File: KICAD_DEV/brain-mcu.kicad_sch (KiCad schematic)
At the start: 22 parts, among them SW1 SW_Push, SW2 SW_Push, U1 STM32H743VITx, Y1 8 MHz, Y2 32.768 KHz

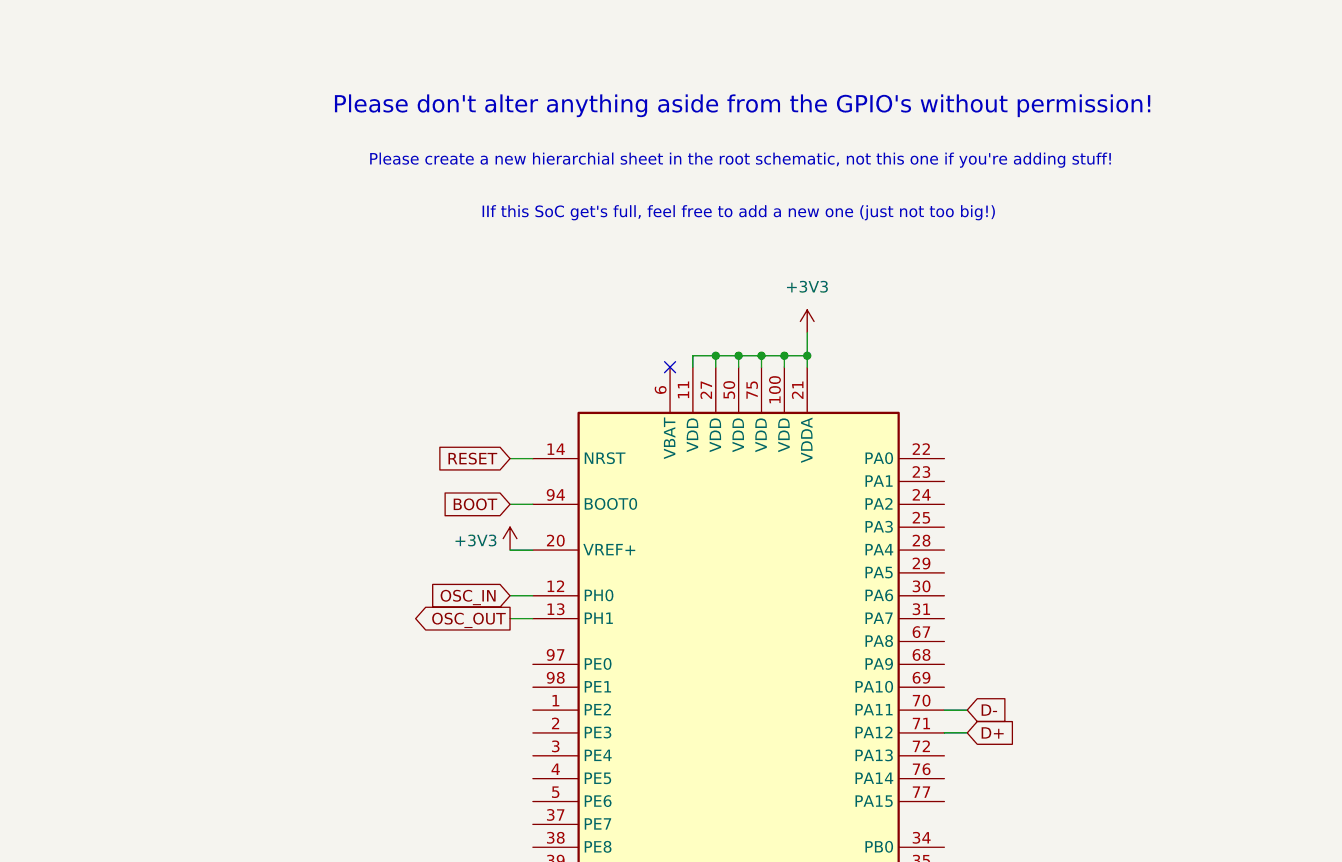
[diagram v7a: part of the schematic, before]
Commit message: wired the TMC2209 to my MCU, also more instructions on the schematic!
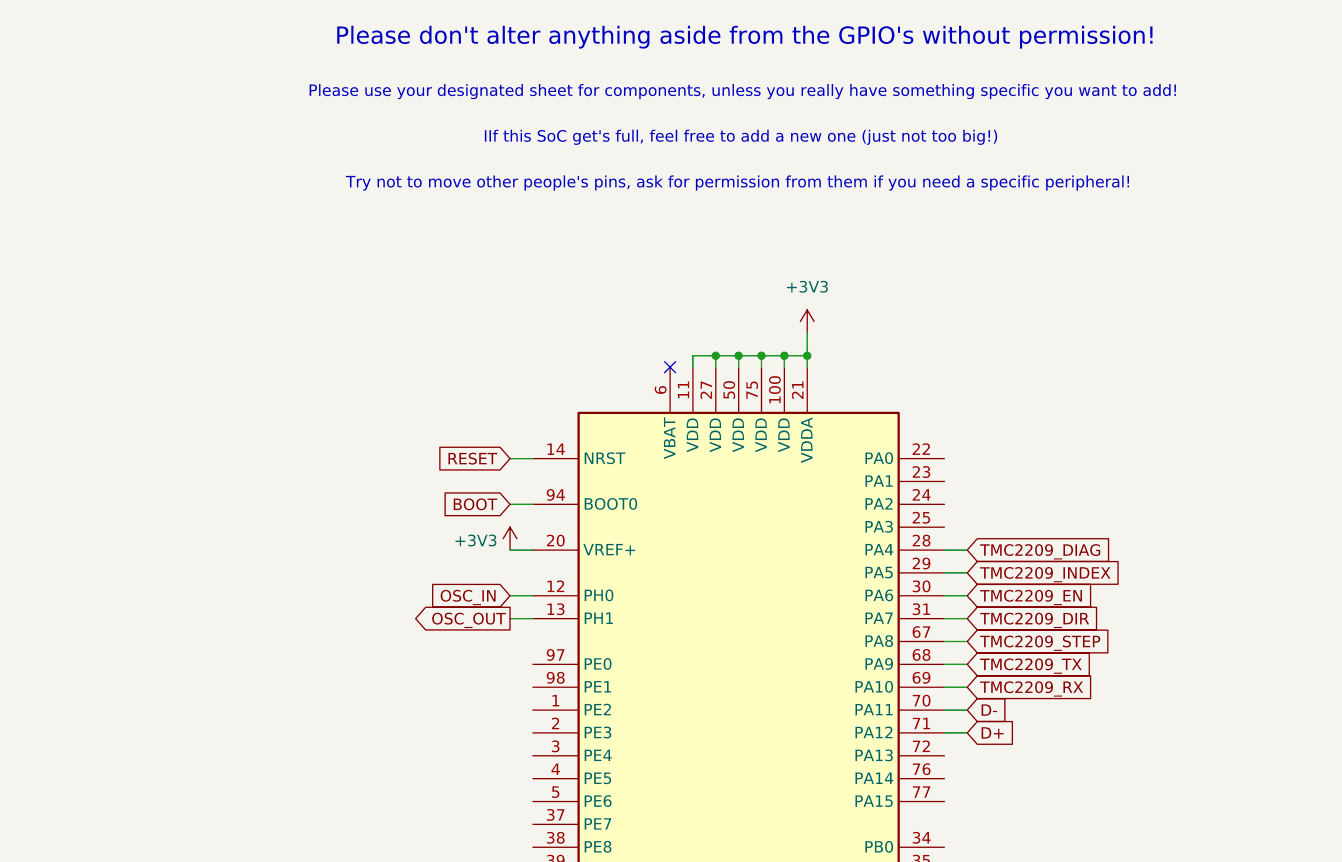
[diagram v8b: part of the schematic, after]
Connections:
- net TMC2209_DIAG: now reaches U1.28 (PA4)
- net TMC2209_INDEX: now reaches U1.29 (PA5)
- net TMC2209_EN: now reaches U1.30 (PA6)
- net TMC2209_DIR: now reaches U1.31 (PA7)
- net TMC2209_STEP: now reaches U1.67 (PA8)
- net TMC2209_TX: now reaches U1.68 (PA9)
- net TMC2209_RX: now reaches U1.69 (PA10)
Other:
- note added: "Please use your designated sheet for components, unless you really have something specific you want to add!"
- note added: "Try not to move other people's pins, ask for permission from them if you need a specific peripheral!"
- note removed: "Please create a new hierarchial sheet in the root schematic, not this one if you're adding stuff!"
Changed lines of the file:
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@@
 	(generator_version "9.0")
 	(paper "A3")
-	(text "Please create a new hierarchial sheet in the root schematic, not this one if you're adding stuff!"
+	(text "Please use your designated sheet for components, unless you really have something specific you want to add!"
 		(exclude_from_sim no)
-		(at 222.504 64.77 0)
+		(at 222.758 57.15 0)
+		(effects
+			(font
+				(size 1.27 1.27)
+			)
+		)
+	)
+	(text "Try not to move other people's pins, ask for permission from them if you need a specific peripheral!"
+		(exclude_from_sim no)
+		(at 222.25 67.31 0)
 		(effects
 			(font
@@
 	(text "IIf this SoC get's full, feel free to add a new one (just not too big!)"
 		(exclude_from_sim no)
-		(at 222.25 70.612 0)
+		(at 222.504 62.23 0)
 		(effects
 			(font
@@
 	(text "Please don't alter anything aside from the GPIO's without permission!"
 		(exclude_from_sim no)
-		(at 222.758 58.674 0)
+		(at 223.012 51.054 0)
 		(effects
 			(font
@@
 	(wire
 		(pts
+			(xy 247.65 107.95) (xy 245.11 107.95)
+		)
+		(stroke
+			(width 0)
+			(type default)
+		)
+	)
+	(wire
+		(pts
 			(xy 60.96 138.43) (xy 63.5 138.43)
 		)
@@
 	(wire
 		(pts
+			(xy 247.65 115.57) (xy 245.11 115.57)
+		)
+		(stroke
+			(width 0)
+			(type default)
+		)
+	)
+	(wire
+		(pts
 			(xy 60.96 217.17) (xy 68.58 217.17)
 		)
@@
 	(wire
 		(pts
+			(xy 247.65 113.03) (xy 245.11 113.03)
+		)
+		(stroke
+			(width 0)
+			(type default)
+		)
+	)
+	(wire
+		(pts
 			(xy 223.52 234.95) (xy 223.52 232.41)
 		)
@@
 	(wire
 		(pts
+			(xy 247.65 123.19) (xy 245.11 123.19)
+		)
+		(stroke
+			(width 0)
+			(type default)
+		)
+	)
+	(wire
+		(pts
 			(xy 57.15 69.85) (xy 64.77 69.85)
 		)
@@
 	(wire
 		(pts
+			(xy 247.65 120.65) (xy 245.11 120.65)
+		)
+		(stroke
+			(width 0)
+			(type default)
+		)
+	)
+	(wire
+		(pts
 			(xy 95.25 69.85) (xy 95.25 68.58)
 		)
@@
 	(wire
 		(pts
+			(xy 247.65 110.49) (xy 245.11 110.49)
+		)
+		(stroke
+			(width 0)
+			(type default)
+		)
+	)
+	(wire
+		(pts
 			(xy 196.85 102.87) (xy 199.39 102.87)
 		)
@@
 	(wire
 		(pts
+			(xy 247.65 118.11) (xy 245.11 118.11)
+		)
+		(stroke
+			(width 0)
+			(type default)
+		)
+	)
+	(wire
+		(pts
 			(xy 184.15 218.44) (xy 194.31 218.44)
 		)
@@
 			(width 0)
 			(type default)
+		)
+	)
+	(global_label "TMC2209_STEP"
+		(shape input)
+		(at 247.65 118.11 0)
+		(fields_autoplaced yes)
+		(effects
+			(font
+				(size 1.27 1.27)
+			)
+			(justify left)
+		)
+		(property "Intersheetrefs" "${INTERSHEET_REFS}"
+			(at 264.7259 118.11 0)
+			(effects
+				(font
+					(size 1.27 1.27)
+				)
+				(justify left)
+				(hide yes)
+			)
 		)
 	)
@@
 		)
 	)
+	(global_label "TMC2209_DIAG"
+		(shape input)
+		(at 247.65 107.95 0)
+		(fields_autoplaced yes)
+		(effects
+			(font
+				(size 1.27 1.27)
+			)
+			(justify left)
+		)
+		(property "Intersheetrefs" "${INTERSHEET_REFS}"
+			(at 264.3632 107.95 0)
+			(effects
+				(font
+					(size 1.27 1.27)
+				)
+				(justify left)
+				(hide yes)
+			)
+		)
+	)
 	(global_label "OSC32_OUT"
 		(shape output)
@@
 		)
 	)
+	(global_label "TMC2209_EN"
+		(shape input)
+		(at 247.65 113.03 0)
+		(fields_autoplaced yes)
+		(effects
+			(font
+				(size 1.27 1.27)
+			)
+			(justify left)
+		)
+		(property "Intersheetrefs" "${INTERSHEET_REFS}"
+			(at 262.6093 113.03 0)
+			(effects
+				(font
+					(size 1.27 1.27)
+				)
+				(justify left)
+				(hide yes)
+			)
+		)
+	)
+	(global_label "TMC2209_TX"
+		(shape input)
+		(at 247.65 120.65 0)
+		(fields_autoplaced yes)
+		(effects
+			(font
+				(size 1.27 1.27)
+			)
+			(justify left)
+		)
+		(property "Intersheetrefs" "${INTERSHEET_REFS}"
+			(at 262.3069 120.65 0)
+			(effects
+				(font
+					(size 1.27 1.27)
+				)
+				(justify left)
+				(hide yes)
+			)
+		)
+	)
 	(global_label "D+"
 		(shape input)
@@
 			(effects
 				(font
+					(size 1.27 1.27)
+				)
+				(justify left)
+				(hide yes)
+			)
+		)
+	)
+	(global_label "TMC2209_DIR"
+		(shape input)
+		(at 247.65 115.57 0)
+		(fields_autoplaced yes)
+		(effects
+			(font
+				(size 1.27 1.27)
+			)
+			(justify left)
+		)
+		(property "Intersheetrefs" "${INTERSHEET_REFS}"
+			(at 263.2746 115.57 0)
+			(effects
+				(font
+					(size 1.27 1.27)
+				)
+				(justify left)
+				(hide yes)
+			)
+		)
+	)
+	(global_label "TMC2209_INDEX"
+		(shape input)
+		(at 247.65 110.49 0)
+		(fields_autoplaced yes)
+		(effects
+			(font
+				(size 1.27 1.27)
+			)
+			(justify left)
+		)
+		(property "Intersheetrefs" "${INTERSHEET_REFS}"
+			(at 265.6936 110.49 0)
+			(effects
+				(font
+					(size 1.27 1.27)
+				)
+				(justify left)
+				(hide yes)
+			)
+		)
+	)
+	(global_label "TMC2209_RX"
+		(shape input)
+		(at 247.65 123.19 0)
+		(fields_autoplaced yes)
+		(effects
+			(font
+				(size 1.27 1.27)
+			)
+			(justify left)
+		)
+		(property "Intersheetrefs" "${INTERSHEET_REFS}"
+			(at 262.6093 123.19 0)
+			(effects
+				(font
